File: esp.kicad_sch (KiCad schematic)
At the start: 26 parts, among them J1 Barrel_Jack, J2 Barrel_Jack_Switch_MountingPin, J3 Barrel_Jack, J4 Barrel_Jack, J5 Barrel_Jack, U1 ESP32-S2-WROVER, U10 34.81-8240, U11 34.81-8240, U12 34.81-9024, U13 34.81-9024, U14 PCF8574ATS, U15 34.81-9024, U16 L298N, U17 PCA9685PW, U2 TCA9548ARGER, U3 TCA9548ARGER, U4 BME280, U5 CCS811, U6 PCF8574ATS, U7 OKI-78SR-12_1.0-W36H-C, U8 OKI-78SR-5_1.5-W36-C, U9 OKI-78SR-3.3_1.5-W36H-C

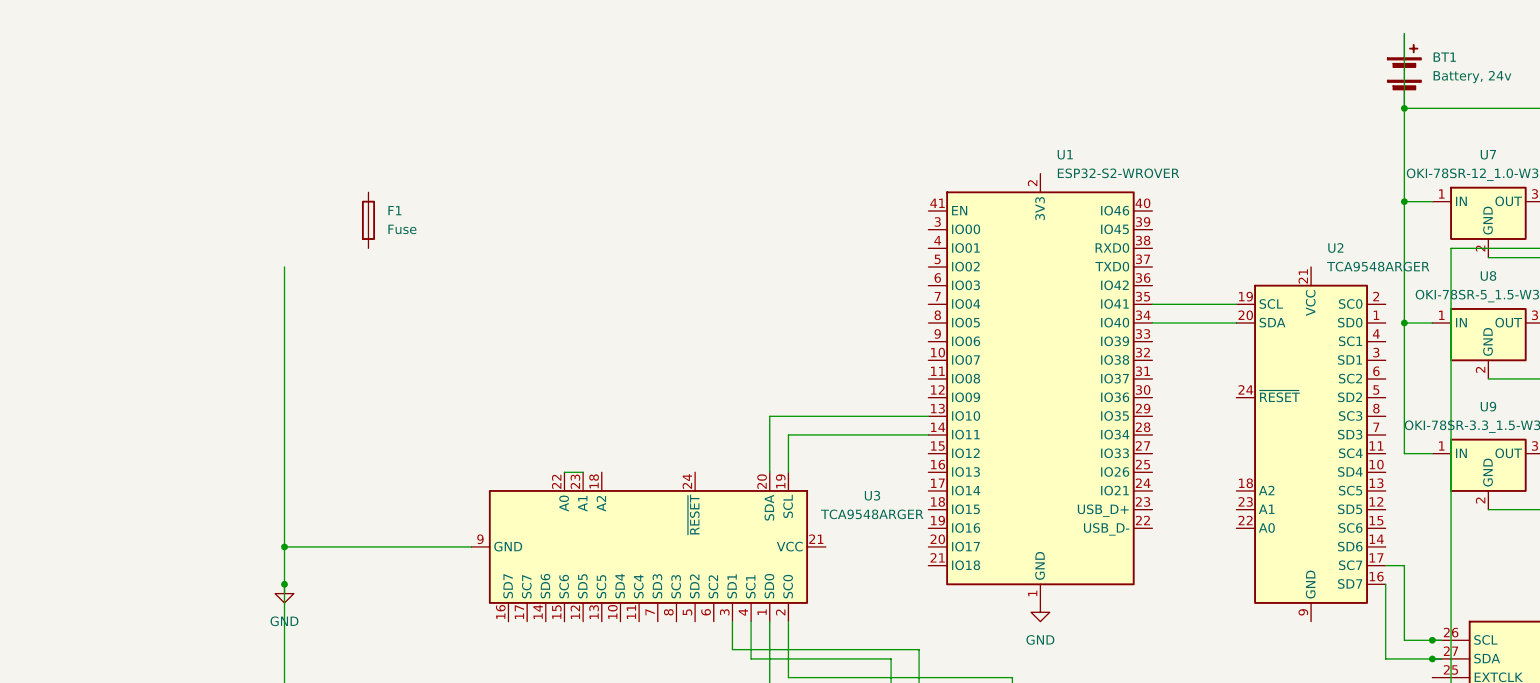
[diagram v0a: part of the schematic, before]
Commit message: added ac/dc plug secondary battery with down
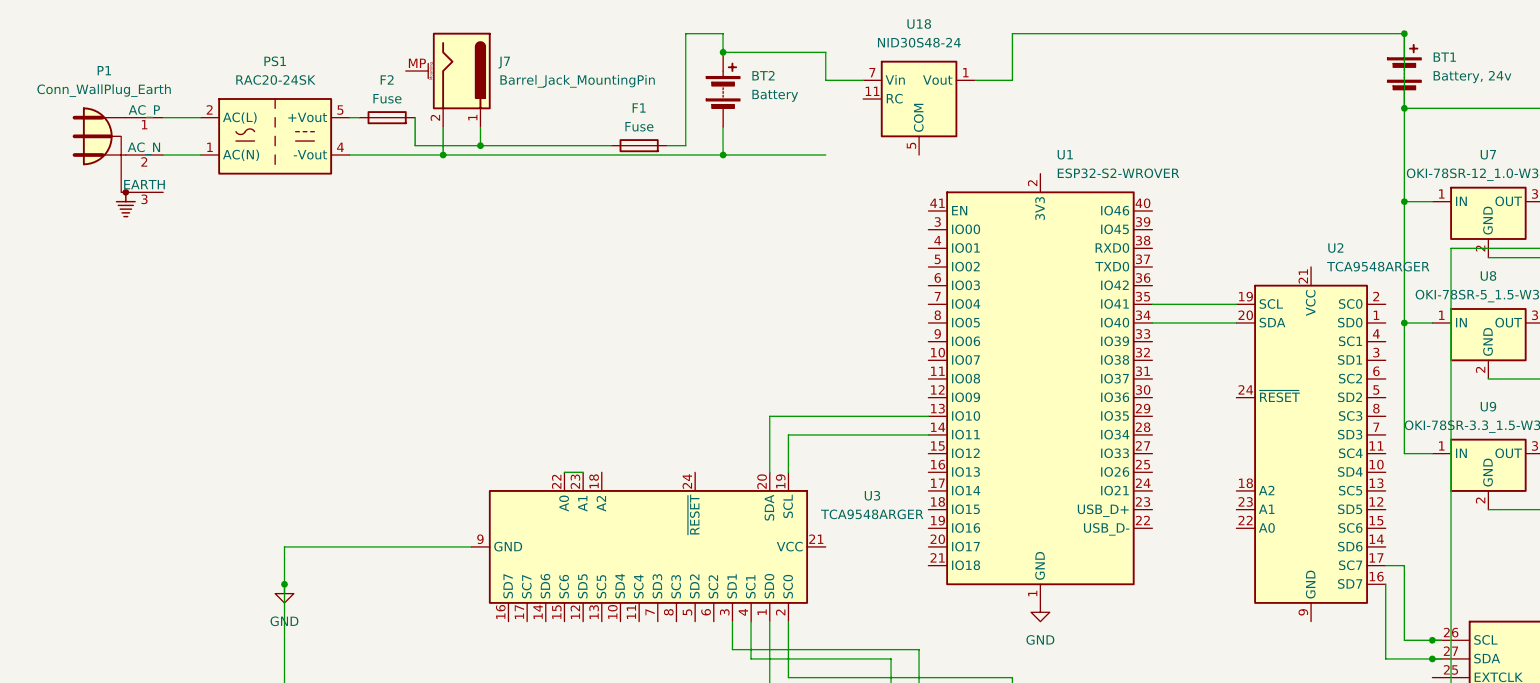
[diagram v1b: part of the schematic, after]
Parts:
- added BT2: Battery, symbol Device:Battery
- added F2: Fuse, symbol Device:Fuse
- added J7: Barrel_Jack_MountingPin, Connector_BarrelJack:BarrelJack_SwitchcraftConxall_RAPC10U_Horizontal, symbol Connector:Barrel_Jack_MountingPin
- added P1: Conn_WallPlug_Earth, symbol Connector:Conn_WallPlug_Earth
- added PS1: RAC20-24SK, Converter_ACDC:Converter_ACDC_Recom_RAC20-xxSK_THT, symbol Converter_ACDC:RAC20-24SK
- added U18: NID30S48-24, Converter_DCDC:Converter_DCDC_MeanWell_NID30_THT, symbol Regulator_Switching:NID30S48-24
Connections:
- net GND: now also U18.1 (Vout), U18.2 (Vout), U18.3 (Vout), U18.4 (Vout)
- net at F1.1: now also F2.2, J7.1
- net at F1.2: now also BT2.1 (+), U18.7 (Vin), U18.8 (Vin)
- new net: F2.1, PS1.5 (+Vout)
- new net: P1.1 (AC_P), PS1.2 (AC(L))
- new net: P1.2 (AC_N), PS1.1 (AC(N))
- new net: BT2.2 (-), J7.2, PS1.4 (-Vout)
- new net: U18.5 (COM), U18.6 (COM)
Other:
- moved on the sheet: F1

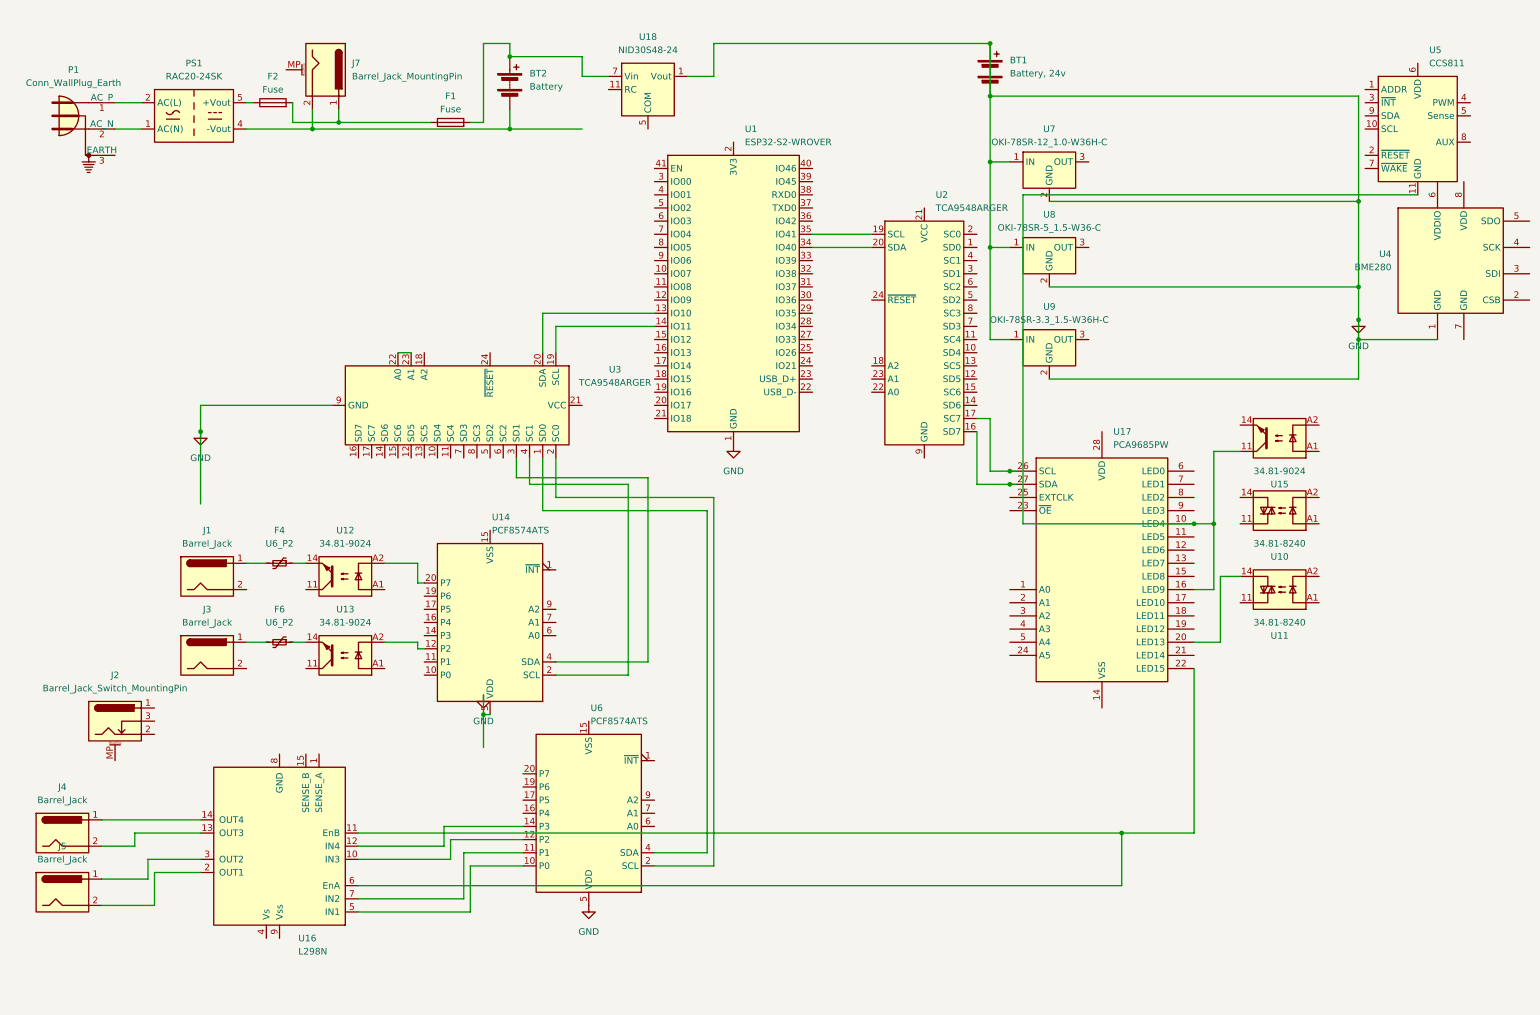
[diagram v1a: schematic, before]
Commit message: added some sheets for detailed view
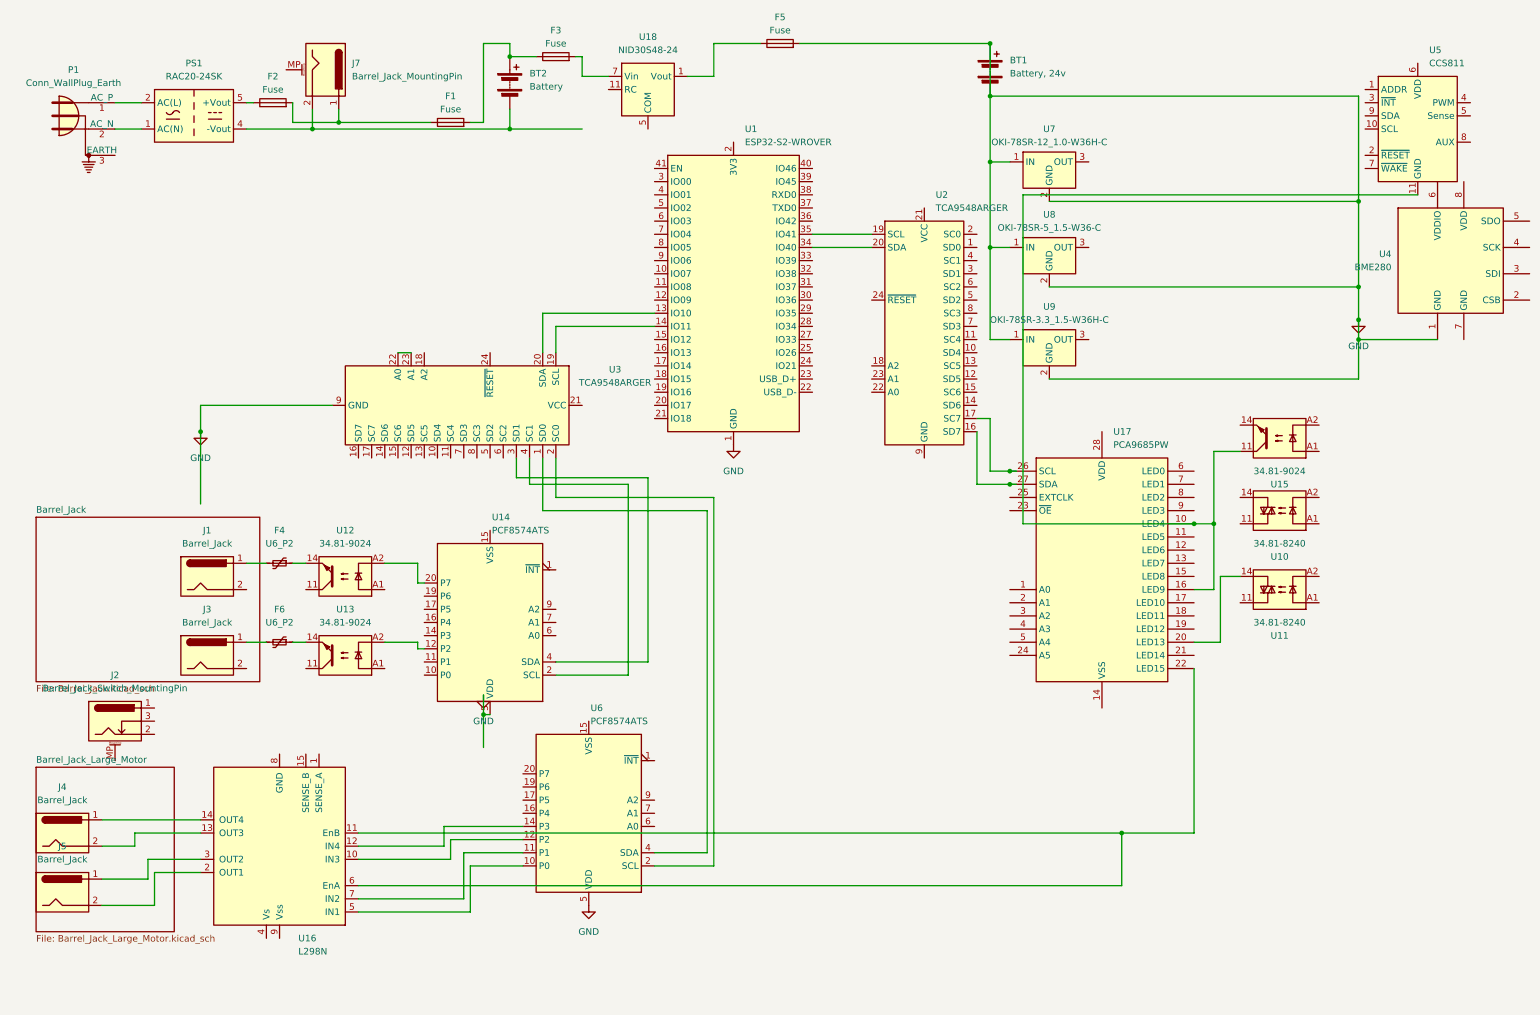
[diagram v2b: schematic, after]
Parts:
- added F3, F5: Fuse, symbol Device:Fuse
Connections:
- net GND: now also F5.2; no longer U18.1 (Vout), U18.2 (Vout), U18.3 (Vout), U18.4 (Vout)
- net at BT2.1 (+), F1.2: now also F3.1; no longer U18.7 (Vin), U18.8 (Vin)
- new net: F3.2, U18.7 (Vin), U18.8 (Vin)
- new net: F5.1, U18.1 (Vout), U18.2 (Vout), U18.3 (Vout), U18.4 (Vout)
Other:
- added sheet Barrel_Jack (Barrel_Jack.kicad_sch)
- added sheet Barrel_Jack_Large_Motor (Barrel_Jack_Large_Motor.kicad_sch)
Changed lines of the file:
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@@
     (stroke (width 0) (type default))
   )
-  (wire (pts (xy 143.51 13.97) (xy 196.85 13.97))
+  (wire (pts (xy 143.51 13.97) (xy 152.4997 13.97))
     (stroke (width 0) (type default))
   )
@@
     (stroke (width 0) (type default))
   )
-  (wire (pts (xy 104.14 16.51) (xy 118.11 16.51))
+  (wire (pts (xy 104.14 16.51) (xy 109.22 16.51))
     (stroke (width 0) (type default))
   )
@@
     (stroke (width 0) (type default))
   )
+  (wire (pts (xy 116.84 16.51) (xy 118.11 16.51))
+    (stroke (width 0) (type default))
+  )
   (wire (pts (xy 34.29 171.45) (xy 34.29 175.26))
     (stroke (width 0) (type default))
@@
   )
   (wire (pts (xy 95.25 179.07) (xy 74.93 179.07))
+    (stroke (width 0) (type default))
+  )
+  (wire (pts (xy 160.1197 13.97) (xy 196.85 13.97))
     (stroke (width 0) (type default))
   )
@@
         (path "/dab6683c-420f-459a-bf9c-0c28b4b081e3"
           (reference "U5") (unit 1)
+        )
+      )
+    )
+  )
+  (symbol (lib_id "Device:Fuse") (at 113.03 16.51 90) (unit 1)
+    (in_bom yes) (on_board yes) (dnp no) (fields_autoplaced)
+    (property "Reference" "F3" (at 113.03 11.43 90)
+      (effects (font (size 1.27 1.27)))
+    )
+    (property "Value" "Fuse" (at 113.03 13.97 90)
+      (effects (font (size 1.27 1.27)))
+    )
+    (property "Footprint" "" (at 113.03 18.288 90)
+      (effects (font (size 1.27 1.27)) hide)
+    )
+    (property "Datasheet" "~" (at 113.03 16.51 0)
+      (effects (font (size 1.27 1.27)) hide)
+    )
+    (pin "1")
+    (pin "2")
+    (instances
+      (project "esp"
+        (path "/dab6683c-420f-459a-bf9c-0c28b4b081e3"
+          (reference "F3") (unit 1)
         )
       )
@@
         (path "/dab6683c-420f-459a-bf9c-0c28b4b081e3"
           (reference "U14") (unit 1)
+        )
+      )
+    )
+  )
+  (symbol (lib_id "Device:Fuse") (at 156.3097 13.97 90) (unit 1)
+    (in_bom yes) (on_board yes) (dnp no) (fields_autoplaced)
+    (property "Reference" "F5" (at 156.3097 8.89 90)
+      (effects (font (size 1.27 1.27)))
+    )
+    (property "Value" "Fuse" (at 156.3097 11.43 90)
+      (effects (font (size 1.27 1.27)))
+    )
+    (property "Footprint" "" (at 156.3097 15.748 90)
+      (effects (font (size 1.27 1.27)) hide)
+    )
+    (property "Datasheet" "~" (at 156.3097 13.97 0)
+      (effects (font (size 1.27 1.27)) hide)
+    )
+    (pin "1")
+    (pin "2")
+    (instances
+      (project "esp"
+        (path "/dab6683c-420f-459a-bf9c-0c28b4b081e3"
+          (reference "F5") (unit 1)
         )
       )
@@
       )
     )
+  )
+  (sheet (at 12.7 153.67) (size 26.67 31.75) (fields_autoplaced)
+    (stroke (width 0.1524) (type solid))
+    (fill (color 0 0 0 0.0000))
+    (property "Sheetname" "Barrel_Jack_Large_Motor" (at 12.7 152.9584 0)
+      (effects (font (size 1.27 1.27)) (justify left bottom))
+    )
+    (property "Sheetfile" "Barrel_Jack_Large_Motor.kicad_sch" (at 12.7 186.0046 0)
+      (effects (font (size 1.27 1.27)) (justify left top))
+    )
+    (instances
+      (project "esp"
+        (path "/dab6683c-420f-459a-bf9c-0c28b4b081e3" (page "3"))
+      )
+    )
+  )
+  (sheet (at 12.7 105.41) (size 43.18 31.75) (fields_autoplaced)
+    (stroke (width 0.1524) (type solid))
+    (fill (color 0 0 0 0.0000))
+    (property "Sheetname" "Barrel_Jack" (at 12.7 104.6984 0)
+      (effects (font (size 1.27 1.27)) (justify left bottom))
+    )
+    (property "Sheetfile" "Barrel_Jack.kicad_sch" (at 12.7 137.7446 0)
+      (effects (font (size 1.27 1.27)) (justify left top))
+    )
+    (instances
+      (project "esp"
+        (path "/dab6683c-420f-459a-bf9c-0c28b4b081e3" (page "2"))
+      )
+    )

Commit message: barrel jack multiple versions, should be turned into branches
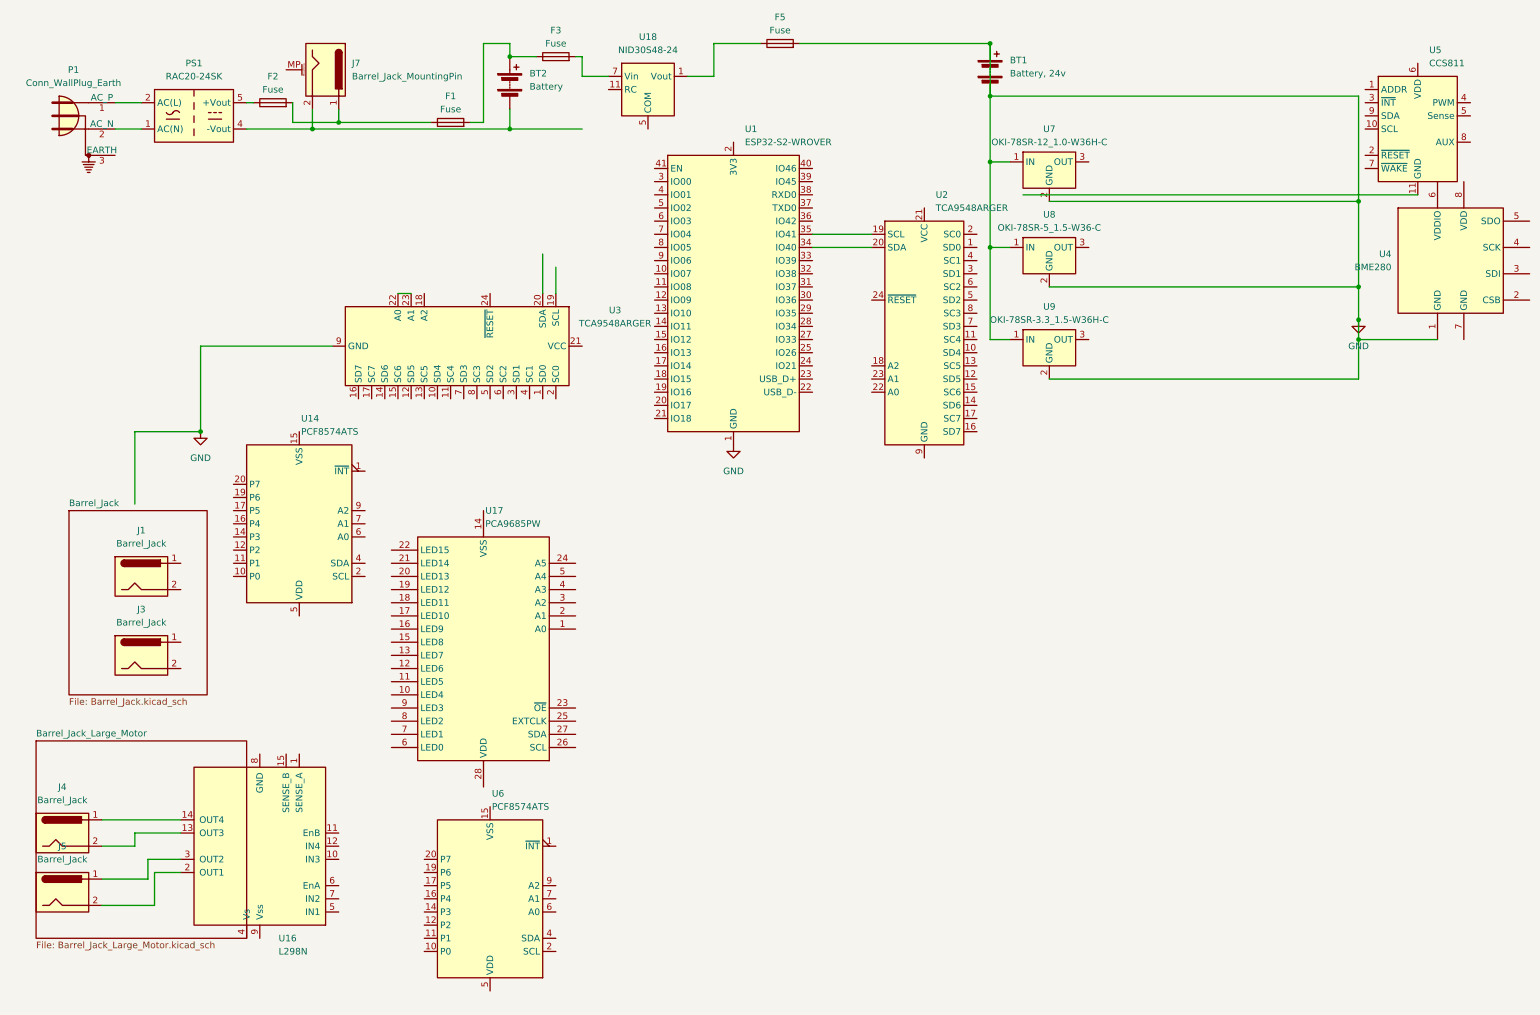
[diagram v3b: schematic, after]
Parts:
- removed F4, F6: U6_P2, symbol Device:Polyfuse_Small
- removed J2: Barrel_Jack_Switch_MountingPin, Connector_BarrelJack:BarrelJack_CUI_PJ-079BH_Horizontal, symbol Connector:Barrel_Jack_Switch_MountingPin
- removed U10, U11: 34.81-8240, OptoDevice:Finder_34.81, symbol Relay_SolidState:34.81-8240
- removed U12, U13, U15: 34.81-9024, OptoDevice:Finder_34.81, symbol Relay_SolidState:34.81-9024
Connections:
- net GND: no longer U14.5 (VDD), U6.5 (VDD)
- net at U17.26 (SCL): no longer U2.17 (SC7)
- net at U17.27 (SDA): no longer U2.16 (SD7)
- net at U3.1 (SD0): no longer U6.4 (SDA)
- net at U3.19 (SCL): no longer U1.14 (IO11)
- net at U3.2 (SC0): no longer U6.2 (SCL)
- net at U3.20 (SDA): no longer U1.13 (IO10)
- net at U3.3 (SD1): no longer U14.4 (SDA)
- net at U3.4 (SC1): no longer U14.2 (SCL)
- net at U6.10 (P0): no longer U16.5 (IN1)
- net at U6.11 (P1): no longer U16.7 (IN2)
- net at U6.12 (P2): no longer U16.10 (IN3)
- net at U6.14 (P3): no longer U16.12 (IN4)
- now unconnected: U16.11 (EnB), U16.6 (EnA), U17.10 (LED4), U17.16 (LED9), U17.22 (LED15), U5.11 (GND)
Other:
- moved on the sheet: J1, J3, U14, U16, U17, U3, U6
